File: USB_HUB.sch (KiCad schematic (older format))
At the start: 23 parts, among them U1 USB2514B_Bi, U2 MIC2026-1BM, U3 MIC2026-1BM, Y1 24 MHz

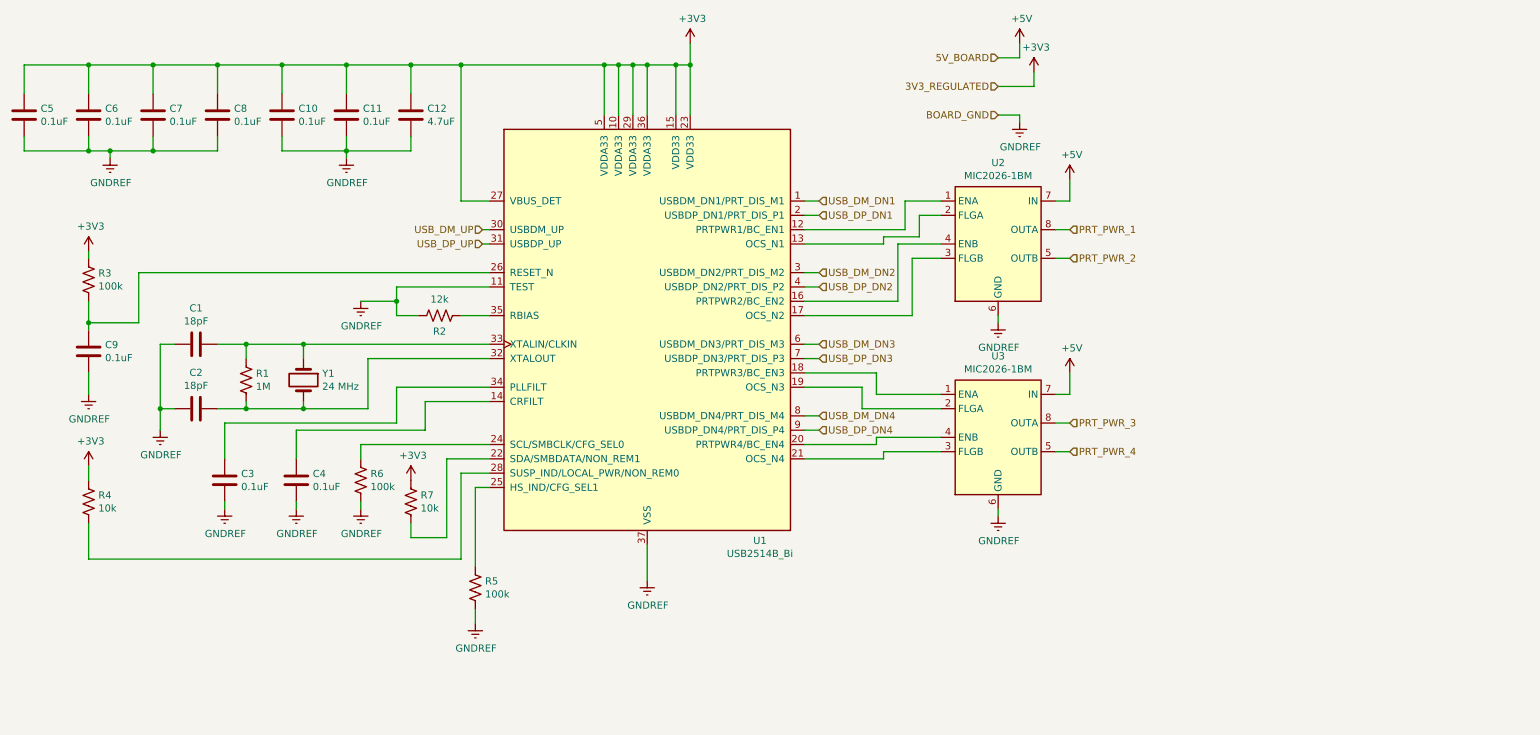
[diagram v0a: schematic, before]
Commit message: Added labels to all components
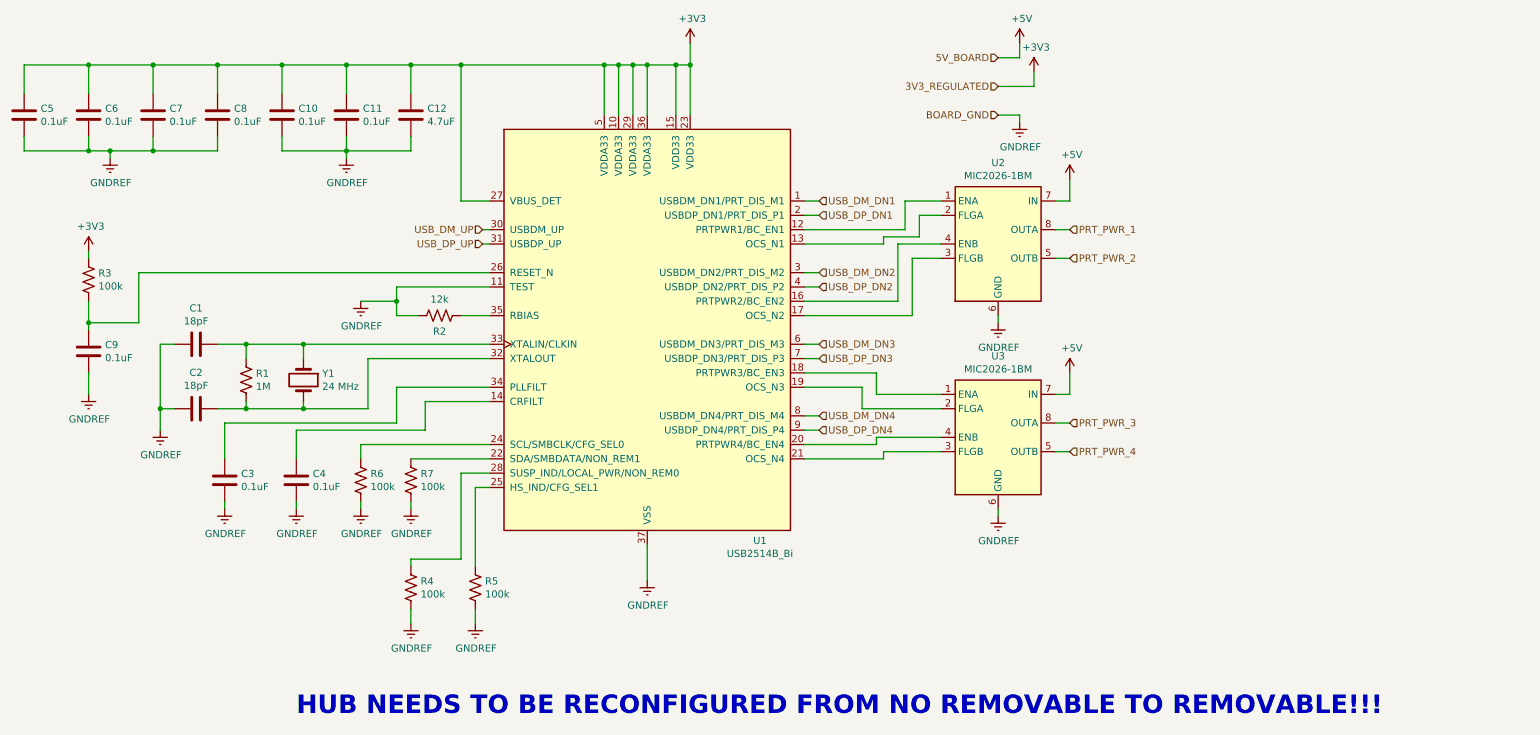
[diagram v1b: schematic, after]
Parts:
- R4, R7: value 10k -> 100k
- U2: footprint (none) -> Package_SO:SOIC-8_3.9x4.9mm_P1.27mm
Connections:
- net +3V3: no longer R4.1, R7.1
- net GNDREF: now also R4.2, R7.2
- net at U1.22 (SDA/SMBDATA/NON_REM1): now also R7.1; no longer R7.2
- net at U1.28 (SUSP_IND/LOCAL_PWR/NON_REM0): now also R4.1; no longer R4.2
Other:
- note added: "HUB NEEDS TO BE RECONFIGURED FROM NO REMOVABLE TO REMOVABLE!!!"
- moved on the sheet: R4, R7
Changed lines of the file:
@@
 encoding utf-8
 Sheet 3 7
-Title "4-Port USB HUB for ISOShield"
+Title "4-Port USB HUB for AvenaShield"
 Date ""
 Rev ""
@@
 F 0 "U2" H 7600 2817 50  0000 C CNN
 F 1 "MIC2026-1BM" H 7600 2726 50  0000 C CNN
-F 2 "" H 7600 2250 50  0001 C CNN
+F 2 "Package_SO:SOIC-8_3.9x4.9mm_P1.27mm" H 7600 2250 50  0001 C CNN
 F 3 "http://ww1.microchip.com/downloads/en/DeviceDoc/mic2026.pdf" H 7600 2250 50  0001 C CNN
 	1    7600 2250
@@
 L Device:R_US R7
 U 1 1 5E6C91D9
-P 3500 4050
-F 0 "R7" H 3568 4096 50  0000 L CNN
-F 1 "10k" H 3568 4005 50  0000 L CNN
-F 2 "" V 3540 4040 50  0001 C CNN
-F 3 "~" H 3500 4050 50  0001 C CNN
-	1    3500 4050
+P 3500 3900
+F 0 "R7" H 3568 3946 50  0000 L CNN
+F 1 "100k" H 3568 3855 50  0000 L CNN
+F 2 "" V 3540 3890 50  0001 C CNN
+F 3 "~" H 3500 3900 50  0001 C CNN
+	1    3500 3900
 	1    0    0    -1
 $EndComp
@@
 Wire Wire Line
 	3150 3650 3150 3750
-$Comp
-L power:+3V3 #PWR0119
-U 1 1 5E7659A2
-P 3500 3900
-F 0 "#PWR0119" H 3500 3750 50  0001 C CNN
-F 1 "+3V3" H 3515 4073 50  0000 C CNN
-F 2 "" H 3500 3900 50  0001 C CNN
-F 3 "" H 3500 3900 50  0001 C CNN
-	1    3500 3900
-	1    0    0    -1
-$EndComp
 Wire Wire Line
 	3150 4050 3150 4100
 Wire Wire Line
-	3500 4200 3500 4300
-Wire Wire Line
-	3500 4300 3750 4300
-Wire Wire Line
-	3750 4300 3750 3750
-Wire Wire Line
-	3750 3750 4050 3750
-Wire Wire Line
-	3850 4450 3850 3850
-Wire Wire Line
 	3850 3850 4050 3850
 Wire Wire Line
 	3950 3950 4050 3950
-$Comp
-L power:+3V3 #PWR0120
-U 1 1 5E889F19
-P 1250 3800
-F 0 "#PWR0120" H 1250 3650 50  0001 C CNN
-F 1 "+3V3" H 1265 3973 50  0000 C CNN
-F 2 "" H 1250 3800 50  0001 C CNN
-F 3 "" H 1250 3800 50  0001 C CNN
-	1    1250 3800
-	1    0    0    -1
-$EndComp
-Wire Wire Line
-	1250 4450 3850 4450
-Wire Wire Line
-	1250 3800 1250 3900
-Wire Wire Line
-	1250 4200 1250 4450
 Wire Wire Line
 	3950 4900 3950 4800
@@
 L Device:R_US R4
 U 1 1 5E5E7009
-P 1250 4050
-F 0 "R4" H 1318 4096 50  0000 L CNN
-F 1 "10k" H 1318 4005 50  0000 L CNN
-F 2 "" V 1290 4040 50  0001 C CNN
-F 3 "~" H 1250 4050 50  0001 C CNN
-	1    1250 4050
+P 3500 4650
+F 0 "R4" H 3568 4696 50  0000 L CNN
+F 1 "100k" H 3568 4605 50  0000 L CNN
+F 2 "" V 3540 4640 50  0001 C CNN
+F 3 "~" H 3500 4650 50  0001 C CNN
+	1    3500 4650
 	1    0    0    -1
 $EndComp
 Wire Wire Line
 	3950 3950 3950 4500
+Text Notes 2700 5550 0    129  ~ 26
+HUB NEEDS TO BE RECONFIGURED FROM NO REMOVABLE TO REMOVABLE!!!
+Wire Wire Line
+	3500 3750 4050 3750
+Wire Wire Line
+	3850 3850 3850 4450
+Wire Wire Line
+	3850 4450 3500 4450
+Wire Wire Line
+	3500 4450 3500 4500
+$Comp
+L power:GNDREF #PWR?
+U 1 1 5E5C69A8
+P 3500 4100
+F 0 "#PWR?" H 3500 3850 50  0001 C CNN
+F 1 "GNDREF" H 3505 3927 50  0000 C CNN
+F 2 "" H 3500 4100 50  0001 C CNN
+F 3 "" H 3500 4100 50  0001 C CNN
+	1    3500 4100
+	1    0    0    -1
+$EndComp
+$Comp
+L power:GNDREF #PWR?
+U 1 1 5E5C6D8B
+P 3500 4900
+F 0 "#PWR?" H 3500 4650 50  0001 C CNN
+F 1 "GNDREF" H 3505 4727 50  0000 C CNN
+F 2 "" H 3500 4900 50  0001 C CNN
+F 3 "" H 3500 4900 50  0001 C CNN
+	1    3500 4900
+	1    0    0    -1
+$EndComp
+Wire Wire Line
+	3500 4050 3500 4100
+Wire Wire Line
+	3500 4800 3500 4900
 $EndSCHEMATC
